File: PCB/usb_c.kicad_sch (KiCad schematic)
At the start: 3 parts

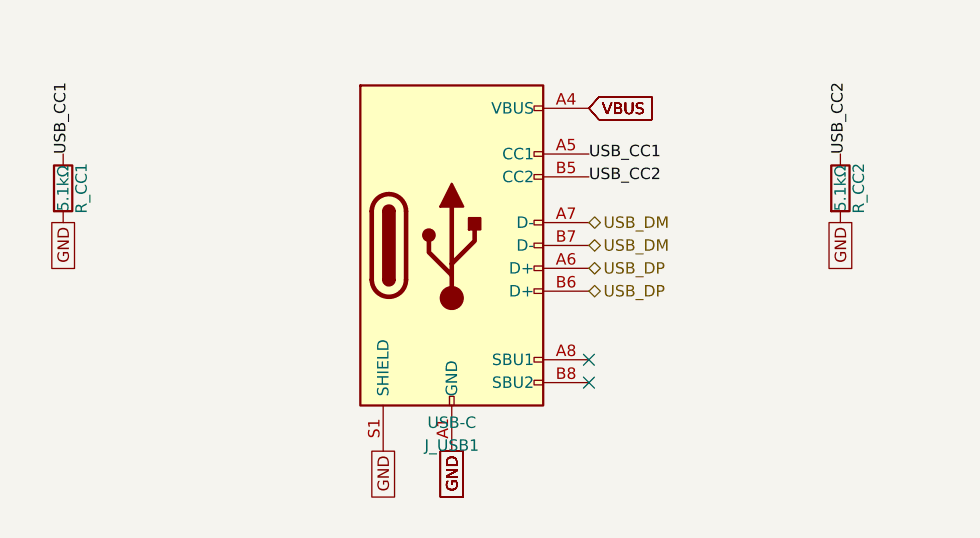
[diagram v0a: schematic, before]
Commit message: Fix footprints and begin layout (#17)
* refactor: updated gulikit footprint

This updates the gulikit thumbstick footprint to be accurate.

* layout: beginning pcb layout

This updates the schematic with a few different footprints while also starts the layout.
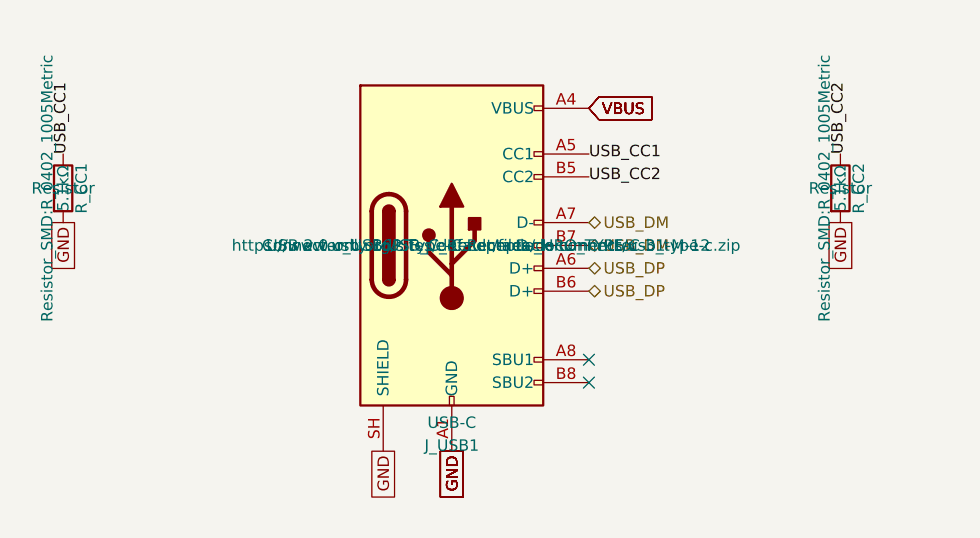
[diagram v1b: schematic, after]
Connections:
- net GND: now also J_USB1.SH (SHIELD); no longer J_USB1.S1 (SHIELD)

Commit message: refactor: swap footprints and add symmetry
This updates the footprints of a couple components to be smaller and closer to what we want. It also adds two buttons to ensure left and right side symmetry.
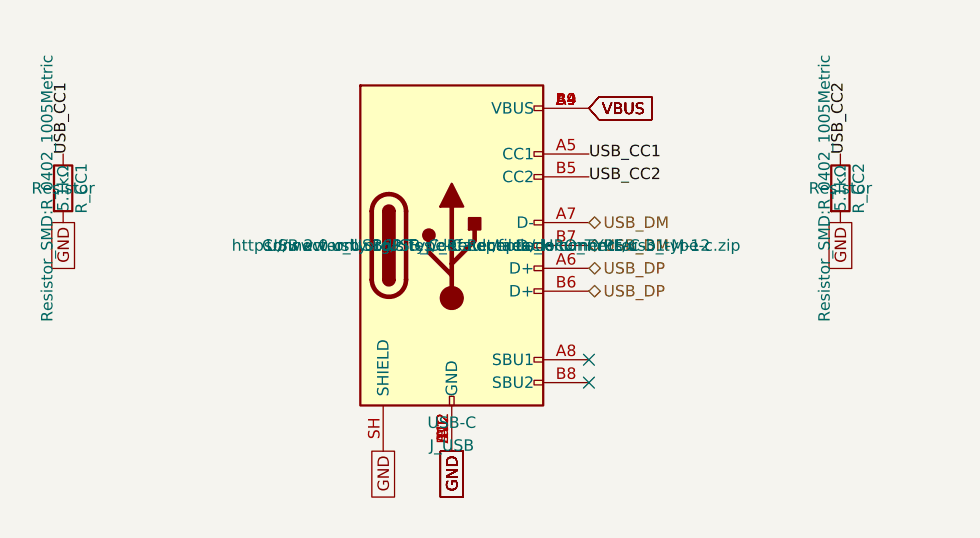
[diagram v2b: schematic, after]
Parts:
- removed J_USB1: USB-C, Connector_USB:USB_C_Receptacle_HRO_TYPE-C-31-M-12, symbol Connector:USB_C_Receptacle_USB2.0_16P
- added J_USB: USB-C, Connector_USB:USB_C_Receptacle_HRO_TYPE-C-31-M-12, symbol Connector:USB_C_Receptacle_USB2.0_16P
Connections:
- net GND: now also J_USB.A1 (GND), J_USB.A12 (GND), J_USB.B1 (GND), J_USB.B12 (GND), J_USB.SH (SHIELD)
- net USB_CC1: now also J_USB.A5 (CC1)
- net USB_CC2: now also J_USB.B5 (CC2)
- net USB_DM: now also J_USB.A7 (D-), J_USB.B7 (D-)
- net USB_DP: now also J_USB.A6 (D+), J_USB.B6 (D+)
- net VBUS: now also J_USB.A4 (VBUS), J_USB.A9 (VBUS), J_USB.B4 (VBUS), J_USB.B9 (VBUS)

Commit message: layout: everything is on the board
The board edge cuts are down to 100mm x 35mm. All the components have the right footprints and are on the board, but no traces exist yet, and not all circuits are laid out properly yet. Lots of DRC warnings.
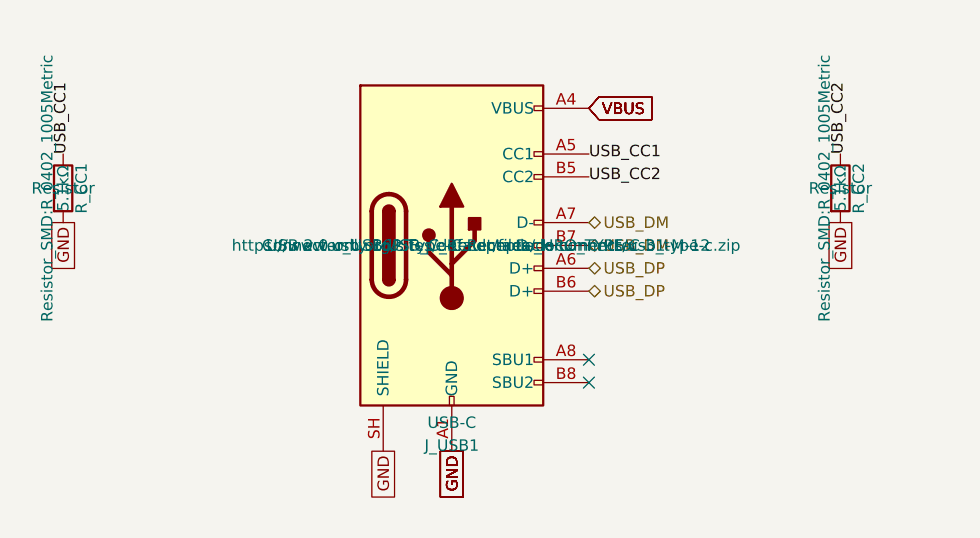
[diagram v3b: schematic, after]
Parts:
- removed J_USB: USB-C, Connector_USB:USB_C_Receptacle_HRO_TYPE-C-31-M-12, symbol Connector:USB_C_Receptacle_USB2.0_16P
- added J_USB1: USB-C, Connector_USB:USB_C_Receptacle_HRO_TYPE-C-31-M-12, symbol Connector:USB_C_Receptacle_USB2.0_16P
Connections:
- net GND: now also J_USB1.A1 (GND), J_USB1.A12 (GND), J_USB1.B1 (GND), J_USB1.B12 (GND), J_USB1.SH (SHIELD)
- net USB_CC1: now also J_USB1.A5 (CC1)
- net USB_CC2: now also J_USB1.B5 (CC2)
- net USB_DM: now also J_USB1.A7 (D-), J_USB1.B7 (D-)
- net USB_DP: now also J_USB1.A6 (D+), J_USB1.B6 (D+)
- net VBUS: now also J_USB1.A4 (VBUS), J_USB1.A9 (VBUS), J_USB1.B4 (VBUS), J_USB1.B9 (VBUS)

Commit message: task: first validation pass
This is the results post first kicad-happy run.
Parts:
- added D_VBUS_TVS1: PESD5V0S1BA, Diode_SMD:D_SOD-323, symbol Device:D_TVS
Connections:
- net GND: now also D_VBUS_TVS1.2 (A2)
- net VBUS: now also D_VBUS_TVS1.1 (A1)
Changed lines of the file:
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@@
+		)
+	)
+	(global_label "GND"
+		(shape passive)
+		(at 179.07 114.3 0)
+		(fields_autoplaced yes)
+		(effects
+			(font
+				(size 1.27 1.27)
+			)
+			(justify left)
+		)
+		(property "Intersheetrefs" "${INTERSHEET_REFS}"
+			(at 179.07 114.3 0)
+			(hide yes)
+			(show_name no)
+			(do_not_autoplace no)
+			(effects
+				(font
+					(size 1.27 1.27)
+				)
+			)
 		)
 	)
@@
 		(property "Intersheetrefs" "${INTERSHEET_REFS}"
 			(at 163.83 92.71 0)
+			(hide yes)
+			(show_name no)
+			(do_not_autoplace no)
+			(effects
+				(font
+					(size 1.27 1.27)
+				)
+			)
+		)
+	)
+	(global_label "VBUS"
+		(shape input)
+		(at 171.45 114.3 180)
+		(fields_autoplaced yes)
+		(effects
+			(font
+				(size 1.27 1.27)
+			)
+			(justify right)
+		)
+		(property "Intersheetrefs" "${INTERSHEET_REFS}"
+			(at 171.45 114.3 0)
 			(hide yes)
 			(show_name no)
@@
 					(unit 1)
 				)
+			)
+		)
+	)
+	(symbol
+		(lib_id "Device:D_TVS")
+		(at 175.26 114.3 0)
+		(unit 1)
+		(body_style 1)
+		(exclude_from_sim no)
+		(in_bom yes)
+		(on_board yes)
+		(in_pos_files yes)
+		(dnp no)
+		(fields_autoplaced yes)
+		(property "Reference" "D_VBUS_TVS1"
+			(at 175 117.54 0)
+			(show_name no)
+			(do_not_autoplace no)
+			(effects
+				(font
+					(size 1.27 1.27)
+				)
+			)
+		)
+		(property "Value" "PESD5V0S1BA"
+			(at 175 112.46 0)
+			(show_name no)
+			(do_not_autoplace no)
+			(effects
+				(font
+					(size 1.27 1.27)
+				)
+			)
+		)
+		(property "Footprint" "Diode_SMD:D_SOD-323"
+			(at 175.26 114.3 0)
+			(show_name no)
+			(do_not_autoplace no)
+			(effects
+				(font
+					(size 1.27 1.27)
+				)
+			)
+		)
+		(property "Datasheet" ""
+			(at 175.26 114.3 0)
+			(show_name no)
+			(do_not_autoplace no)
+			(effects
+				(font
+					(size 1.27 1.27)
+				)
+			)
+		)
+		(property "Description" "Bidirectional transient-voltage-suppression diode"
+			(at 175.26 114.3 0)
+			(show_name no)
+			(do_not_autoplace no)
+			(effects
+				(font
+					(size 1.27 1.27)
+				)
+			)
+		)
+		(pin "1"
+		)
+		(pin "2"
+		)
+		(instances
+			(project "snips_controller"
+				(path "/21935953-32a0-46ad-8079-8177920c6978/a79dce81-618b-4a1c-ac71-81a6b4c28e48"
+					(reference "D_VBUS_TVS1")
+					(unit 1)
+				)

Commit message: task: part number populated (#26)
kicad-happy run part 2 - MPN numbers populated
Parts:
- D_VBUS_TVS1: MF (none) -> Nexperia; Manufacturer_Part_Number (none) -> PESD5V0S1BA,115
- J_USB1: MF (none) -> Hroparts Elec; Manufacturer_Part_Number (none) -> TYPE-C-31-M-12
- R_CC1, R_CC2: MF (none) -> Yageo; Manufacturer_Part_Number (none) -> RC0402FR-075K1L
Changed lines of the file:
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@@
+			)
+		)
+		(property "MF" "Hroparts Elec" (at 0 0 0)
+			(effects
+				(font
+					(size 1.27 1.27)
+				)
+				(hide yes)
+			)
+		)
+		(property "Manufacturer_Part_Number" "TYPE-C-31-M-12" (at 0 0 0)
+			(effects
+				(font
+					(size 1.27 1.27)
+				)
+				(hide yes)
 			)
 		)
@@
 			)
 		)
+		(property "MF" "Yageo" (at 0 0 0)
+			(effects
+				(font
+					(size 1.27 1.27)
+				)
+				(hide yes)
+			)
+		)
+		(property "Manufacturer_Part_Number" "RC0402FR-075K1L" (at 0 0 0)
+			(effects
+				(font
+					(size 1.27 1.27)
+				)
+				(hide yes)
+			)
+		)
 		(pin "1"
 		)
@@
 			)
 		)
+		(property "MF" "Yageo" (at 0 0 0)
+			(effects
+				(font
+					(size 1.27 1.27)
+				)
+				(hide yes)
+			)
+		)
+		(property "Manufacturer_Part_Number" "RC0402FR-075K1L" (at 0 0 0)
+			(effects
+				(font
+					(size 1.27 1.27)
+				)
+				(hide yes)
+			)
+		)
 		(pin "1"
 		)
@@
 			)
 		)
+		(property "MF" "Nexperia" (at 0 0 0)
+			(effects
+				(font
+					(size 1.27 1.27)
+				)
+				(hide yes)
+			)
+		)
+		(property "Manufacturer_Part_Number" "PESD5V0S1BA,115" (at 0 0 0)
+			(effects
+				(font
+					(size 1.27 1.27)
+				)
+				(hide yes)
+			)
+		)
